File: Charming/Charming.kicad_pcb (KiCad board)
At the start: 2 copper layers, 275.5 x 80.8 mm, 97 parts, among them SW1 SW_Push, SW10 SW_Push, SW11 SW_Push, SW12 SW_Push, SW13 SW_Push, SW14 SW_Push, SW15 SW_Push, SW16 SW_Push, SW17 SW_Push, SW18 SW_Push, SW19 SW_Push, SW2 SW_Push, SW20 SW_Push, SW21 SW_Push, SW22 SW_Push, SW23 SW_Push, SW24 SW_Push, SW25 SW_Push, SW26 SW_Push, SW27 SW_Push, SW28 SW_Push, SW29 SW_Push, SW3 SW_Push, SW30 SW_Push, SW31 SW_Push, SW32 SW_Push, SW33 SW_Push, SW34 SW_Push, SW35 SW_Push, SW36 SW_Push, SW37 SW_Push, SW38 SW_Push, SW39 SW_Push, SW4 SW_Push, SW40 SW_Push, SW41 SW_Push, SW42 SW_Push, SW43 SW_Push, SW44 SW_Push, SW45 SW_Push, SW46 SW_Push, SW47 SW_Push, SW48 SW_Push, SW5 SW_Push, SW6 SW_Push, SW7 SW_Push, SW8 SW_Push, SW9 SW_Push, U1 ProMicro

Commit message: v2
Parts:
- moved U1 5.31 mm to (19.0, 85.5)
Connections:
- U1 pad 10: col5 -> col3
- U1 pad 13: col6 -> col4
- U1 pad 14: col7 -> col5
- U1 pad 15: row1 -> col6
- U1 pad 16: col8 -> col7
- U1 pad 17: col9 -> col8
- U1 pad 18: col10 -> col9
- U1 pad 19: col11 -> col10
- U1 pad 20: row0 -> col11
- U1 pad 5: col0 -> row0
- U1 pad 6: col1 -> row1
- U1 pad 7: col2 -> col0
- U1 pad 8: col3 -> col1
- U1 pad 9: col4 -> col2
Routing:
- net col4: track 180.4 -> 157.1 mm
- net col5: track 191.8 -> 171.2 mm
- net row0: track 246.1 -> 257.6 mm
- net row1: track 248.2 -> 258.5 mm
- net col3: track 163.4 -> 154.0 mm
- net col2: track 143.4 -> 135.9 mm
- net col0: track 104.2 -> 97.2 mm
- net col10: track 283.0 -> 276.3 mm
- net col11: track 301.3 -> 294.8 mm
- net col1: track 123.3 -> 117.0 mm
- net row3: track 286.0 -> 280.3 mm
- net row2: track 271.0 -> 265.2 mm
- net col7: track 230.5 -> 225.2 mm
- net col8: track 247.2 -> 242.2 mm
- net col6: track 216.7 -> 211.7 mm
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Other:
- board size 275.5 x 80.8 mm -> 270.8 x 80.8 mm
- board text added: "Charming 40 Kit by James Sa Rev2, June 2020"

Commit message: even odd pins
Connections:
- U1 pad 10: col3 -> col9
- U1 pad 11: row2 -> col11
- U1 pad 13: col4 -> row2
- U1 pad 14: col5 -> col10
- U1 pad 15: col6 -> col8
- U1 pad 16: col7 -> row1
- U1 pad 17: col8 -> col6
- U1 pad 18: col9 -> col4
- U1 pad 19: col10 -> col2
- U1 pad 20: col11 -> col0
- U1 pad 21: (no net) -> VCC
- U1 pad 6: row1 -> col1
- U1 pad 7: col0 -> col3
- U1 pad 8: col1 -> col5
- U1 pad 9: col2 -> col7
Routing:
- net col5: track 171.2 -> 191.9 mm
- net col9: track 257.4 -> 277.3 mm
- net col11: track 294.8 -> 314.7 mm
- net row2: track 265.2 -> 248.9 mm
- net row1: track 258.5 -> 243.4 mm
- net col0: track 97.2 -> 84.3 mm
- net col2: track 135.9 -> 123.3 mm
- net col7: track 225.2 -> 237.7 mm
- net col4: track 157.1 -> 163.4 mm
- net col6: track 211.7 -> 206.0 mm
- net col3: track 154.0 -> 158.6 mm
- net col10: track 276.3 -> 280.2 mm
- net col1: track 117.0 -> 119.6 mm
- net col8: track 242.2 -> 242.8 mm
- added copper zone on F.Cu, net VCC

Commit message: v2
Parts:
- moved D42 12.3 mm to (157.8, 116.1)
- moved D1 9.54 mm to (53.2, 63.9)
- moved D10 9.54 mm to (224.2, 63.9)
- moved D11 9.54 mm to (243.2, 63.9)
- moved D12 9.54 mm to (262.2, 63.9)
- moved D13 9.54 mm to (48.5, 82.9)
- moved D14 9.54 mm to (67.5, 82.9)
- moved D15 9.54 mm to (86.5, 82.9)
- moved D16 9.54 mm to (105.5, 82.9)
- moved D17 9.54 mm to (124.5, 82.9)
- moved D18 9.54 mm to (143.5, 82.9)
- moved D19 9.54 mm to (172.0, 82.9)
- moved D2 9.54 mm to (72.2, 63.9)
- moved D20 9.54 mm to (191.0, 82.9)
- moved D21 9.54 mm to (210.0, 82.9)
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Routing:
- net row3: track 280.6 -> 266.5 mm
- net Net-(D42-Pad2): track 10.3 -> 7.09 mm
- net row2: track 248.9 -> 250.0 mm

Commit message: Kicad routing practice
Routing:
- net col7: track 237.7 -> 241.2 mm
- net col9: track 277.3 -> 279.4 mm
- net col8: track 242.8 -> 245.0 mm
- net col11: track 314.7 -> 316.8 mm
- net col10: track 280.2 -> 282.3 mm

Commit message: bump
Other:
- board text added: "Charming 40 Kit by James Sa Rev2.1, July 2020"
- board text removed: "Charming 40 Kit by James Sa Rev2, June 2020"

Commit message: new layout
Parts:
- removed D10, D11, D12, D13, D14, D15, D16, D17, D18, D19, D20, D21, D22, D23, D24, D25, D26, D27, D28, D29, D30, D31, D32, D33, D34, D35, D36, D37, D38, D39, D40, D41, D42, D43, D44, D45, D46, D47, D48, D8, D9: D, Diode_SMD:D_SOD-123
- removed SW10, SW11, SW12, SW13, SW14, SW15, SW16, SW17, SW18, SW19, SW20, SW21, SW22, SW23, SW24, SW25, SW26, SW27, SW28, SW29, SW30, SW31, SW32, SW33, SW34, SW35, SW36, SW37, SW38, SW39, SW40, SW41, SW42, SW43, SW44, SW45, SW46, SW47, SW48, SW5, SW6, SW7, SW8, SW9: SW_Push, Charming:SW_PG1350
- added Boot1: Boot, Button_Switch_THT:SW_PUSH_6mm, F.Cu at (131.6, 82.9)
- added C1: 4.7u, Capacitor_THT:CP_Radial_D4.0mm_P1.50mm, F.Cu at (39.6, 97.5)
- added C2: 0.1u, Capacitor_THT:C_Disc_D4.3mm_W1.9mm_P5.00mm, F.Cu at (86.6, 95.0)
- added C3: 0.1u, Capacitor_THT:C_Disc_D4.3mm_W1.9mm_P5.00mm, F.Cu at (91.7, 82.5)
- added C4: 22pf, Capacitor_THT:C_Disc_D3.0mm_W1.6mm_P2.50mm, F.Cu at (103.6, 97.0)
- added C5: 22pf, Capacitor_THT:C_Disc_D3.0mm_W1.6mm_P2.50mm, F.Cu at (84.1, 97.3)
- added F1: 100mA, Fuse:Fuse_Bourns_MF-RG700, F.Cu at (46.5, 100.1)
- added J1: AVR-ISP-6, Keebio:ICSP-Header, F.Cu at (112.8, 84.8)
- added R1: 10k, Resistor_THT:R_Axial_DIN0204_L3.6mm_D1.6mm_P5.08mm_Horizontal, F.Cu at (65.0, 94.7)
- added R2: 1.5K, Resistor_THT:R_Axial_DIN0204_L3.6mm_D1.6mm_P5.08mm_Horizontal, F.Cu at (65.0, 97.3)
- added R3: 5.1K, Resistor_THT:R_Axial_DIN0204_L3.6mm_D1.6mm_P5.08mm_Horizontal, F.Cu at (65.0, 85.1)
- added R4: 5.1K, Resistor_THT:R_Axial_DIN0204_L3.6mm_D1.6mm_P5.08mm_Horizontal, F.Cu at (65.0, 92.5)
- added R5: 75, Resistor_THT:R_Axial_DIN0204_L3.6mm_D1.6mm_P5.08mm_Horizontal, F.Cu at (65.0, 90.2)
- added R6: 75, Resistor_THT:R_Axial_DIN0204_L3.6mm_D1.6mm_P5.08mm_Horizontal, F.Cu at (59.9, 87.9)
- added Reset1: Reset, Button_Switch_THT:SW_PUSH_6mm, F.Cu at (142.2, 82.8)
- added USB1: HRO-TYPE-C-31-M-12, Keebio:HRO-TYPE-C-31-M-12-Assembly, F.Cu at (31.8, 88.6)
- added Y1: 16MHz, Crystal:Crystal_HC49-4H_Vertical, F.Cu at (91.4, 96.6)
- D1: value D -> LED; footprint Diode_SMD:D_SOD-123 -> LED_THT:LED_D3.0mm
- D2, D3: value D -> 3.6V; footprint Diode_SMD:D_SOD-123 -> Diode_THT:D_DO-35_SOD27_P7.62mm_Horizontal
- D4, D5, D6, D7: footprint Diode_SMD:D_SOD-123 -> Diode_THT:D_DO-35_SOD27_P7.62mm_Horizontal
- SW1, SW2, SW3, SW4: footprint Charming:SW_PG1350 -> Button_Switch_Keyboard:SW_Cherry_MX_1.00u_PCB
- U1: value ProMicro -> ATmega328P-PU; footprint Keebio:ArduinoProMicro -> Package_DIP:DIP-28_W7.62mm
- moved SW2 70.4 mm to (127.0, 112.9)
- moved SW1 69.5 mm to (106.8, 112.9)
- moved SW4 66.6 mm to (127.0, 133.1)
- moved SW3 66.3 mm to (106.8, 133.1)
- moved D7 56.7 mm to (117.6, 91.3), turned to 270 degrees
- moved D3 49.5 mm to (46.5, 85.1), turned to 0 degrees
- moved U1 45.9 mm to (71.4, 92.6), turned to 90 degrees
- moved D6 45.5 mm to (112.0, 91.5), turned to 270 degrees
- moved D1 38.3 mm to (35.1, 97.5)
- moved D2 36.8 mm to (46.5, 90.2), turned to 0 degrees
- moved D5 28.8 mm to (120.4, 91.3), turned to 270 degrees
- moved D4 28.0 mm to (114.8, 91.5), turned to 270 degrees
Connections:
- net VCC renamed Net-(U1-Pad21)
- D1 pad 1: row0 -> GND
- D2 pad 1: row0 -> Net-(D2-Pad1)
- D2 pad 2: Net-(D2-Pad2) -> GND
- D3 pad 1: row0 -> Net-(D3-Pad1)
- D3 pad 2: Net-(D3-Pad2) -> GND
- D4 pad 1: row0 -> Row0
- D5 pad 1: row0 -> Row1
- D6 pad 1: row0 -> Row0
- D7 pad 1: row0 -> Row1
- SW1 pad 1: col0 -> Col0
- SW1 pad 2: Net-(D1-Pad2) -> Net-(D4-Pad2)
- SW2 pad 1: col1 -> Col0
- SW2 pad 2: Net-(D2-Pad2) -> Net-(D5-Pad2)
- SW3 pad 1: col2 -> Col1
- SW3 pad 2: Net-(D3-Pad2) -> Net-(D6-Pad2)
- SW4 pad 1: col3 -> Col1
- SW4 pad 2: Net-(D4-Pad2) -> Net-(D7-Pad2)
- U1 pad 1: (no net) -> Reset
- U1 pad 10: col9 -> Net-(C4-Pad2)
- U1 pad 11: col11 -> Boot
- U1 pad 12: row3 -> Net-(U1-Pad12)
- U1 pad 13: row2 -> Net-(U1-Pad13)
- U1 pad 14: col10 -> Net-(U1-Pad14)
- U1 pad 15: col8 -> Net-(U1-Pad15)
- U1 pad 16: row1 -> Net-(U1-Pad16)
- U1 pad 17: col6 -> Mosi
- U1 pad 18: col4 -> Miso
- U1 pad 19: col2 -> Sck
- U1 pad 2: (no net) -> Net-(U1-Pad2)
- U1 pad 20: col0 -> +5V
- U1 pad 22: (no net) -> GND
- U1 pad 23: GND -> Row0
- U1 pad 24: (no net) -> Row1
- U1 pad 3: GND -> Net-(U1-Pad3)
- U1 pad 4: GND -> D+
- U1 pad 5: row0 -> D-
- U1 pad 6: col1 -> Net-(U1-Pad6)
- U1 pad 7: col3 -> +5V
- U1 pad 8: col5 -> GND
- U1 pad 9: col7 -> Net-(C5-Pad2)
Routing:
- net col11: track 316.8 -> 0.00 mm
- net col10: track 282.3 -> 0.00 mm
- net col9: track 279.4 -> 0.00 mm
- net row3: track 266.5 -> 0.00 mm
- net row0: track 257.6 -> 0.00 mm
- net row2: track 250.0 -> 0.00 mm
- net col8: track 245.0 -> 0.00 mm
- net row1: track 243.4 -> 0.00 mm
- net col7: track 241.2 -> 0.00 mm
- net col6: track 206.4 -> 0.00 mm
- net col5: track 191.9 -> 0.00 mm
- net col4: track 163.4 -> 0.00 mm
- net col3: track 158.6 -> 0.00 mm
- net col2: track 123.3 -> 0.00 mm
- net col1: track 119.6 -> 0.00 mm
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- added copper zone on F.Cu, net +5V
- removed copper zone on F.Cu, net Net-(U1-Pad21)
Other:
- board outline removed
- net class Default: clearance 0.127 -> 0.2; trace_width 0.127 -> 0.25; via_dia 0.6 -> 0.8; via_drill 0.3 -> 0.4
- net class Power: trace_width 0.2 -> 0.5; via_dia 0.6 -> 0.8; via_drill 0.3 -> 0.4
- rule pad_to_mask_clearance: 0 -> 0.05
- rule trace_clearance: 0.127 -> 0.2
- rule trace_min: 0.127 -> 0.2
- rule via_min_size: 0.6 -> 0.4
- board text removed: "Charming 40 Kit by James Sa Rev2.1, July 2020"

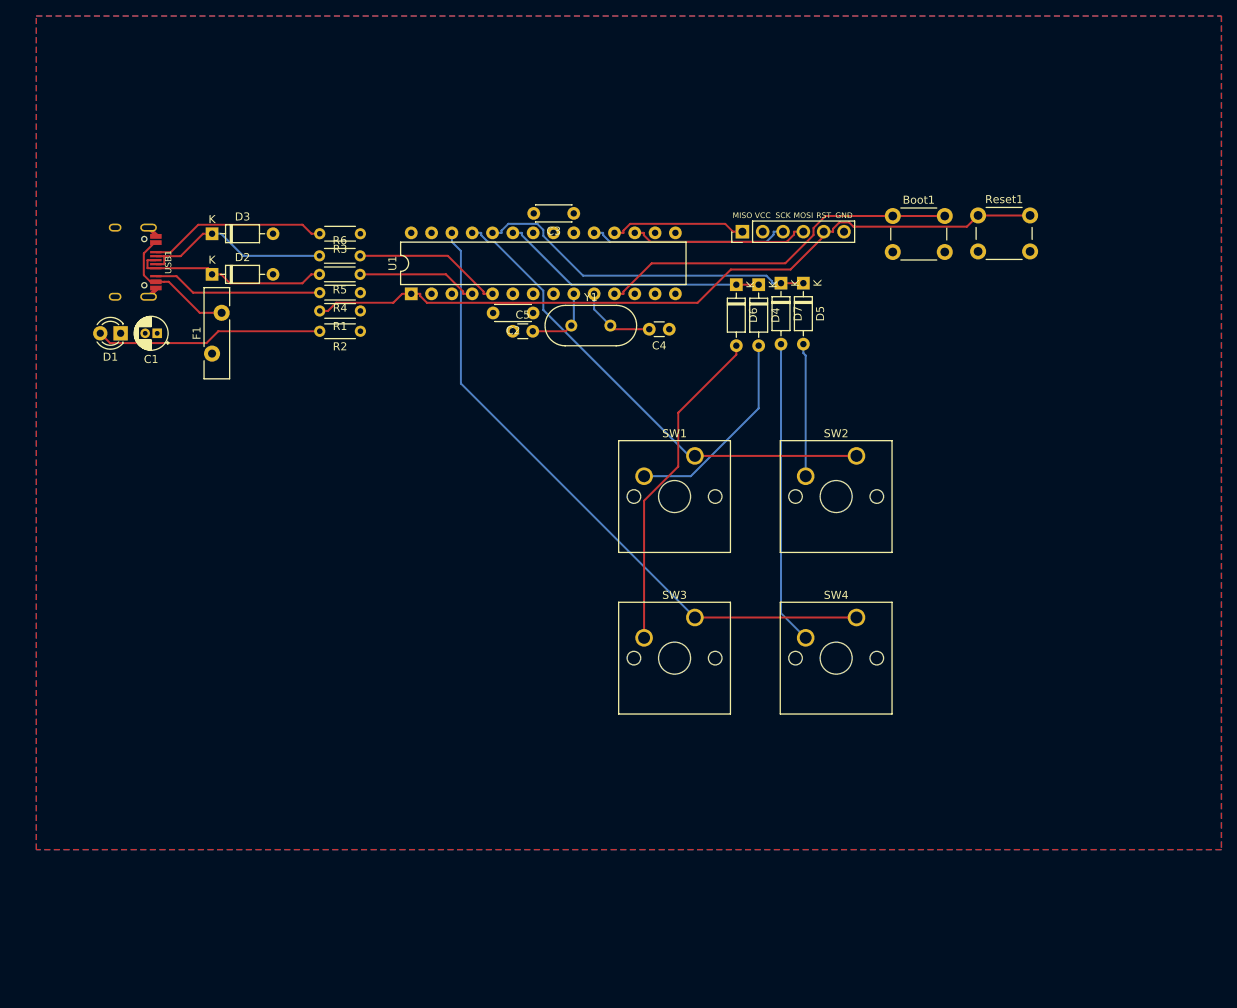
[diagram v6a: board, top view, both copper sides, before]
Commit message: customize symbol and footprint
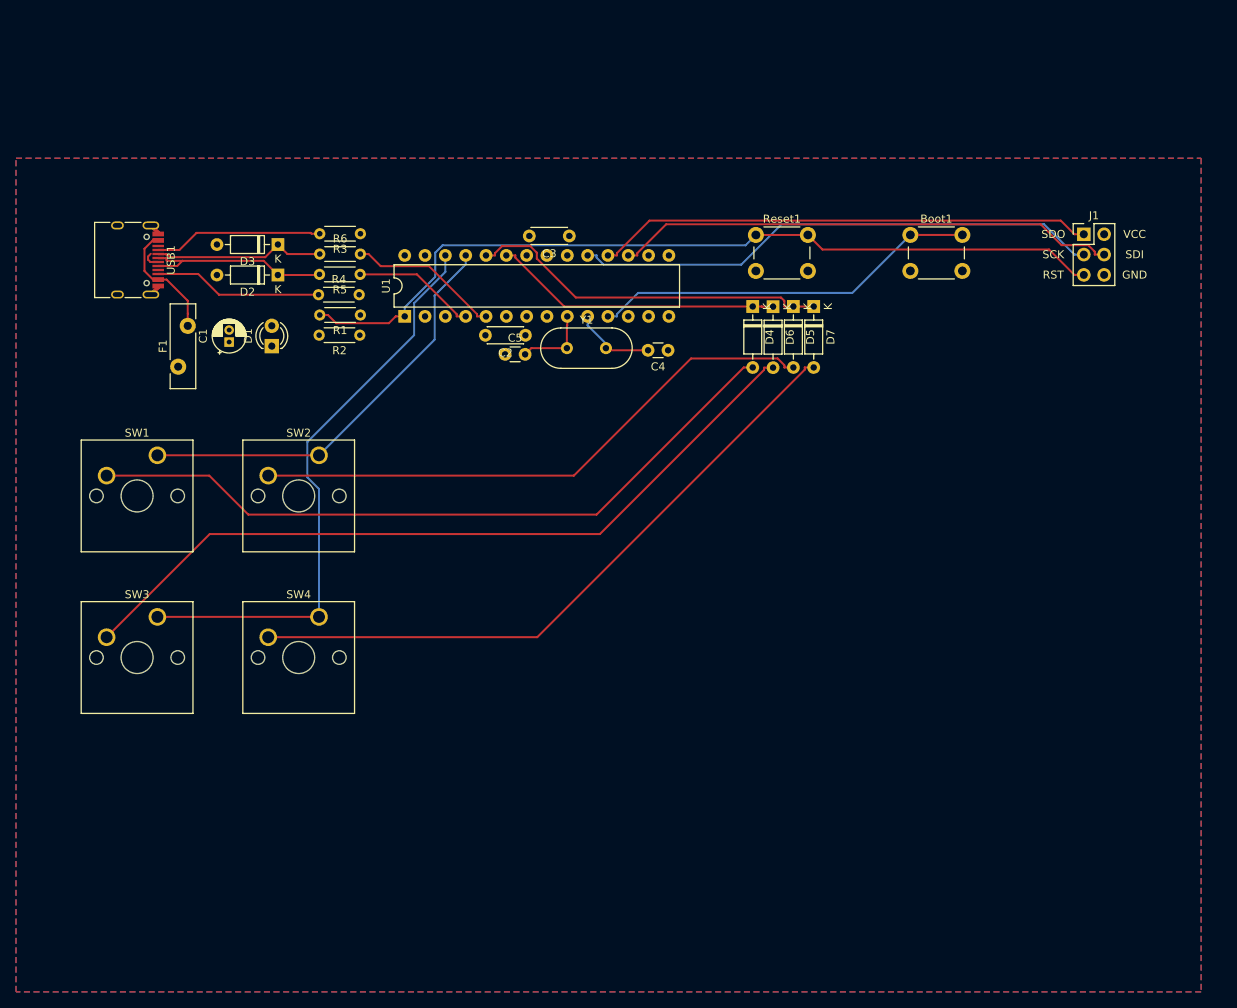
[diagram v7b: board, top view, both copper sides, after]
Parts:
- F1: footprint Fuse:Fuse_Bourns_MF-RG700 -> Fuse:Fuse_Bourns_MF-RG500
- J1: value AVR-ISP-6 -> AVR ISP; footprint Keebio:ICSP-Header -> Charming:AVRISP
- USB1: value HRO-TYPE-C-31-M-12 -> TYPE-C; footprint Keebio:HRO-TYPE-C-31-M-12-Assembly -> Charming:USB_C_Receptacle_HRO_TYPE-C-31-M-12
- moved SW2 67.2 mm to (59.9, 112.8)
- moved SW4 67.2 mm to (59.9, 133.0)
- moved SW1 67.2 mm to (39.7, 112.8)
- moved SW3 67.2 mm to (39.7, 133.0)
- moved J1 42.7 mm to (155.5, 85.2), turned to 0 degrees
- moved Reset1 27.9 mm to (114.5, 85.2)
- moved D1 19.0 mm to (54.0, 99.1), turned to 90 degrees
- moved C1 9.06 mm to (48.6, 98.6), turned to 90 degrees
- moved D3 8.34 mm to (54.7, 86.4), turned to 180 degrees
- moved D2 8.23 mm to (54.7, 90.3), turned to 180 degrees
- moved D6 5.35 mm to (116.6, 94.2)
- moved R4 5.24 mm to (59.8, 92.7), turned to 0 degrees
- moved D7 5.02 mm to (121.7, 94.2)
- moved F1 4.54 mm to (42.2, 101.7)
- moved USB1 3.95 mm to (35.7, 88.4)
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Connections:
- net Miso renamed SDO
- net Mosi renamed SDI
- net Sck renamed SCK
- R4 pad 1: GND -> Net-(R4-Pad1)
- R4 pad 2: Net-(R4-Pad2) -> GND
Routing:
- net Net-(D4-Pad2): track 25.7 -> 90.4 mm
- net Net-(D6-Pad2): track 41.3 -> 97.4 mm
- net Net-(D5-Pad2): track 16.6 -> 72.3 mm
- net SDO: track 17.0 -> 62.2 mm
- net Net-(D7-Pad2): track 38.0 -> 82.3 mm
- net SCK: track 25.0 -> 66.3 mm
- net SDI: track 22.4 -> 63.0 mm
- net Net-(D1-Pad2): track 28.6 -> 0.00 mm
- net Net-(R4-Pad2): track 21.3 -> 0.00 mm
- net Net-(R4-Pad1): track 0.00 -> 21.1 mm
- net Reset: track 96.1 -> 105.0 mm
- net Col0: track 61.2 -> 52.8 mm
- net Col1: track 80.9 -> 73.1 mm
- net Boot: track 46.0 -> 48.7 mm
- net Row0: track 33.6 -> 36.2 mm
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- added copper zone on F.Cu, net GND
- removed copper zone on F.Cu, net +5V
